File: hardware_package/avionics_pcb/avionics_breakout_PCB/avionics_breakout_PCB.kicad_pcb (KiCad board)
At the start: 2 copper layers, 5 parts, among them SW1 SW_Push

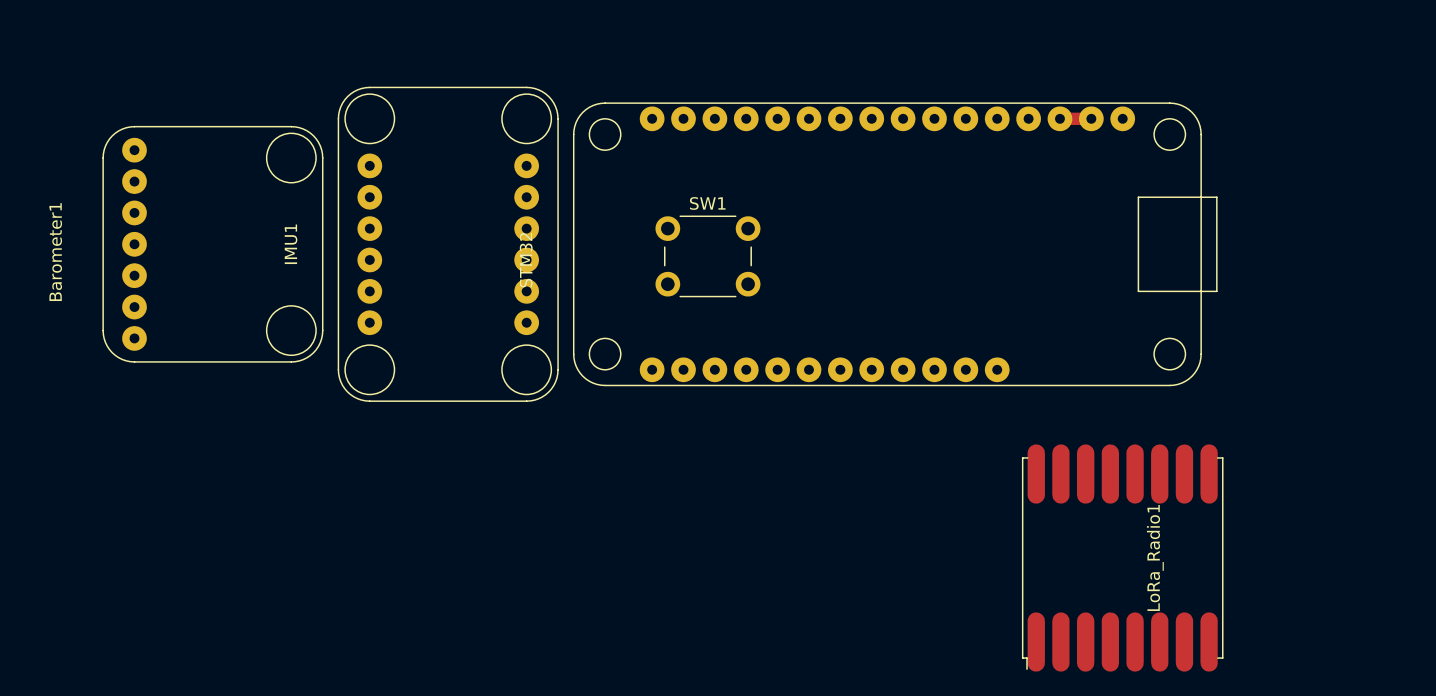
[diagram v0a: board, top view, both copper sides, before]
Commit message: Completed the PCB for the breakout board based avionics board. Also updated the CI/CD to include this new PCB
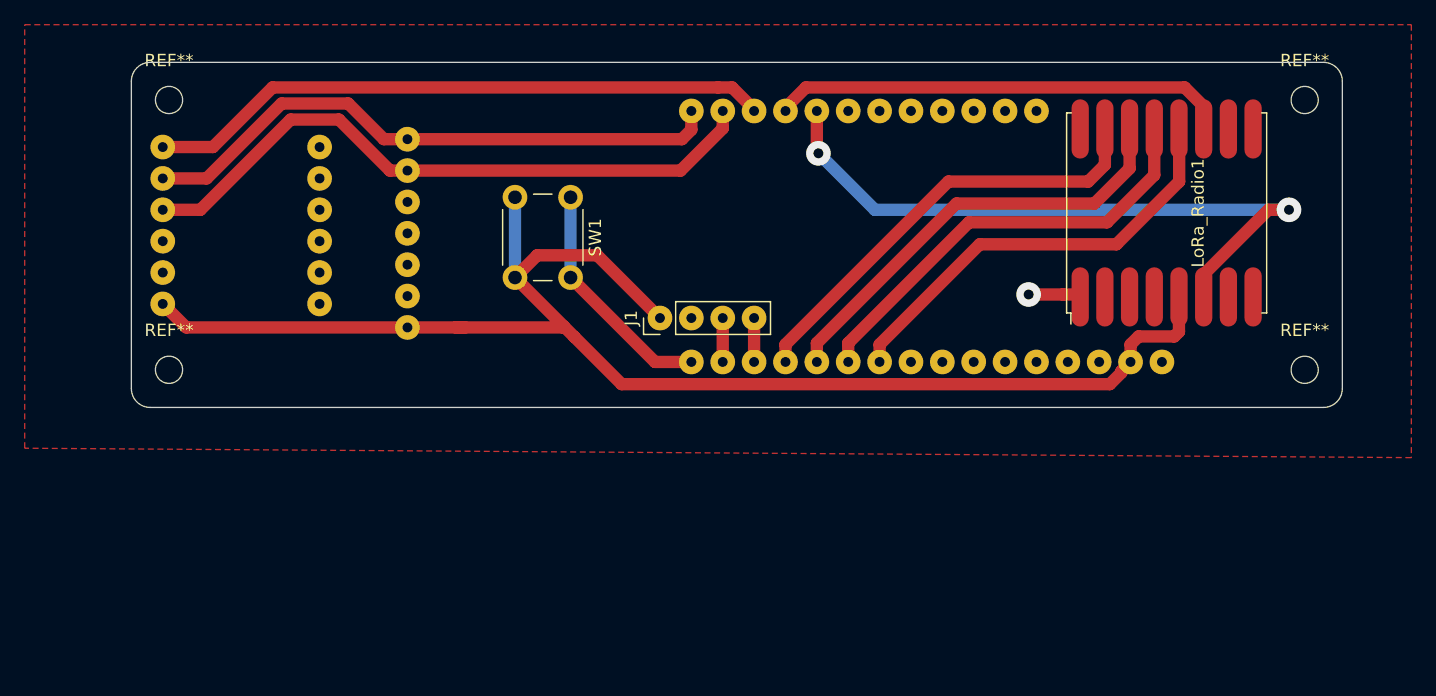
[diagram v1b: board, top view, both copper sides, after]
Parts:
- added J1: GPS, Connector_PinHeader_2.54mm:PinHeader_1x04_P2.54mm_Vertical, F.Cu at (76.8, 107.6)
- added REF**: MountingHole_2.2mm_M2, MountingHole:MountingHole_2.2mm_M2, F.Cu at (129.0, 111.8)
- added REF**: MountingHole_2.2mm_M2, MountingHole:MountingHole_2.2mm_M2, F.Cu at (129.0, 89.9)
- added REF**: MountingHole_2.2mm_M2, MountingHole:MountingHole_2.2mm_M2, F.Cu at (37.1, 89.9)
- added REF**: MountingHole_2.2mm_M2, MountingHole:MountingHole_2.2mm_M2, F.Cu at (37.1, 111.8)
- Barometer1, IMU1, STM32: moved to B.Cu
- moved LoRa_Radio1 28.2 mm to (117.9, 99.1)
- moved Barometer1 22.2 mm to (64.0, 100.1), turned to 90 degrees
- moved IMU1 16.8 mm to (41.7, 100.1), turned to 90 degrees
- moved SW1 8.27 mm to (69.6, 97.8), turned to 270 degrees
- moved STM32 3.24 mm to (69.2, 101.0), turned to 90 degrees
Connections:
- Barometer1 pad 1: 3V3 -> +3V3
- Barometer1 pad 3: Net-(Barometer1-Pad3) -> (no net)
- Barometer1 pad 4: Net-(Barometer1-Pad4) -> (no net)
- Barometer1 pad 5: Net-(Barometer1-Pad5) -> (no net)
- IMU1 pad 1: 3V3 -> +3V3
- IMU1 pad 10: Net-(IMU1-Pad10) -> (no net)
- IMU1 pad 11: Net-(IMU1-Pad11) -> (no net)
- IMU1 pad 12: Net-(IMU1-Pad12) -> (no net)
- IMU1 pad 2: Net-(IMU1-Pad2) -> (no net)
- IMU1 pad 6: Net-(IMU1-Pad6) -> INT_IMU
- IMU1 pad 7: Net-(IMU1-Pad7) -> GND
- IMU1 pad 8: Net-(IMU1-Pad8) -> (no net)
- IMU1 pad 9: Net-(IMU1-Pad9) -> (no net)
- LoRa_Radio1 pad 1: Net-(LoRa_Radio1-Pad1) -> (no net)
- LoRa_Radio1 pad 10: Net-(LoRa_Radio1-Pad10) -> (no net)
- LoRa_Radio1 pad 11: Net-(LoRa_Radio1-Pad11) -> RESET
- LoRa_Radio1 pad 12: Net-(LoRa_Radio1-Pad12) -> CS
- LoRa_Radio1 pad 13: Net-(LoRa_Radio1-Pad13) -> SCK
- LoRa_Radio1 pad 14: Net-(LoRa_Radio1-Pad14) -> MOSI
- LoRa_Radio1 pad 15: Net-(LoRa_Radio1-Pad15) -> MISO
- LoRa_Radio1 pad 16: Net-(LoRa_Radio1-Pad16) -> GND
- LoRa_Radio1 pad 3: Net-(LoRa_Radio1-Pad3) -> (no net)
- LoRa_Radio1 pad 4: Net-(LoRa_Radio1-Pad4) -> (no net)
- LoRa_Radio1 pad 5: 3V3 -> +3V3
- LoRa_Radio1 pad 6: Net-(LoRa_Radio1-Pad6) -> INT_LORA
- LoRa_Radio1 pad 7: Net-(LoRa_Radio1-Pad7) -> (no net)
- LoRa_Radio1 pad 8: Net-(LoRa_Radio1-Pad8) -> (no net)
- LoRa_Radio1 pad 9: Net-(LoRa_Radio1-Pad9) -> GND
- STM32 pad 1: Net-(STM32-Pad1) -> (no net)
- STM32 pad 10: Net-(STM32-Pad10) -> CS
- STM32 pad 11: Net-(STM32-Pad11) -> SCK
- STM32 pad 12: Net-(STM32-Pad12) -> MOSI
- STM32 pad 13: Net-(STM32-Pad13) -> MISO
- STM32 pad 14: Net-(STM32-Pad14) -> RX
- STM32 pad 15: Net-(STM32-Pad15) -> TX
- STM32 pad 19: Net-(STM32-Pad19) -> INT_IMU
- STM32 pad 2: 3V3 -> +3V3
- STM32 pad 20: Net-(STM32-Pad20) -> RESET
- STM32 pad 21: Net-(STM32-Pad21) -> INT_LORA
- STM32 pad 22: Net-(STM32-Pad22) -> (no net)
- STM32 pad 23: Net-(STM32-Pad23) -> (no net)
- STM32 pad 24: Net-(STM32-Pad24) -> (no net)
- STM32 pad 25: Net-(STM32-Pad25) -> (no net)
- STM32 pad 26: Net-(STM32-Pad26) -> (no net)
- STM32 pad 27: Net-(STM32-Pad27) -> (no net)
- STM32 pad 28: Net-(STM32-Pad28) -> (no net)
- STM32 pad 3: 3V3 -> (no net)
- STM32 pad 5: Net-(STM32-Pad5) -> (no net)
- STM32 pad 6: Net-(STM32-Pad6) -> (no net)
- STM32 pad 7: Net-(STM32-Pad7) -> (no net)
- STM32 pad 8: Net-(STM32-Pad8) -> (no net)
- STM32 pad 9: Net-(STM32-Pad9) -> (no net)
- SW1 pad 2: 3V3 -> +3V3
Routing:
- net +3V3: track 0.00 -> 116.7 mm
- net INT_LORA: track 0.00 -> 55.6 mm, vias 0 -> 2
- net SCL: track 0.00 -> 52.9 mm
- net INT_IMU: track 0.00 -> 50.7 mm
- net SDA: track 0.00 -> 48.3 mm
- net SCK: track 0.00 -> 37.6 mm
- net MISO: track 0.00 -> 37.4 mm
- net MOSI: track 0.00 -> 37.2 mm
- net CS: track 0.00 -> 36.6 mm
- net RESET: track 0.00 -> 36.2 mm
- net Boot: track 0.00 -> 19.1 mm
- net (no net): track 0.00 -> 5.51 mm, vias 0 -> 1
- net GND: track 0.00 -> 5.41 mm
- net TX: track 0.00 -> 3.56 mm
- net RX: track 0.00 -> 3.56 mm
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- added copper zone on F.Cu, net GND
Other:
- board outline added: 98 x 27.9 mm

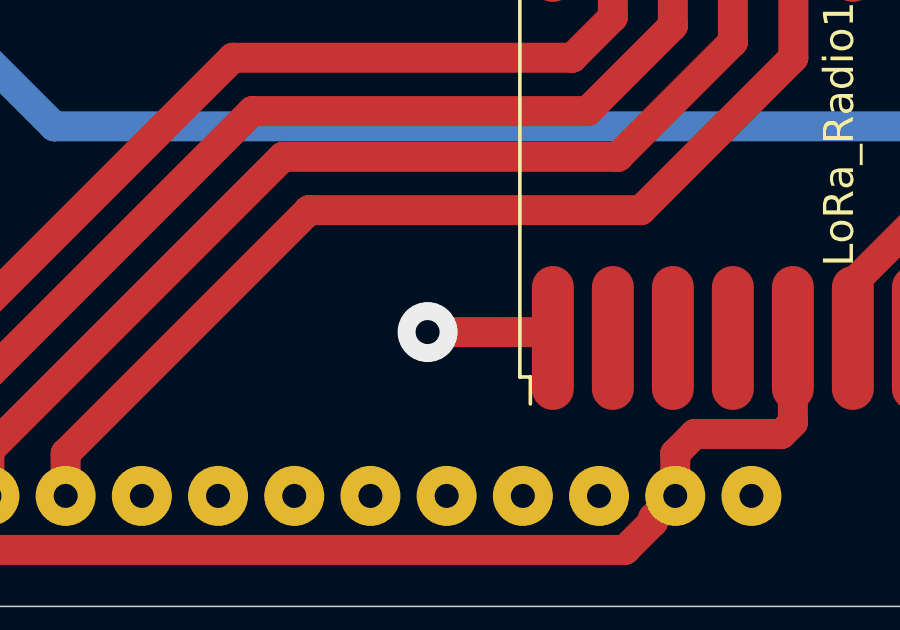
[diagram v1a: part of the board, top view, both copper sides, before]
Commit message: Fixed DRC check errors
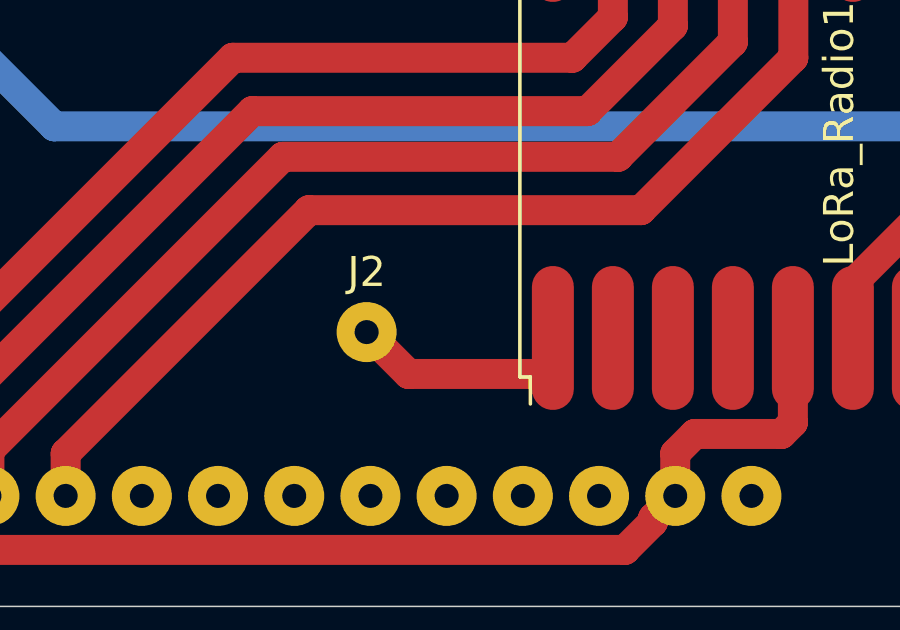
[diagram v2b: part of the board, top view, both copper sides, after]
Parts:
- added J2: ANT, Connector_Wire:SolderWire-0.1sqmm_1x01_D0.4mm_OD1mm, F.Cu at (104.6, 105.7)
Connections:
- LoRa_Radio1 pad 1: (no net) -> Net-(J2-Pad1)
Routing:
- net Net-(J2-Pad1): track 0.00 -> 6.79 mm
- net (no net): track 5.51 -> 0.00 mm, vias 1 -> 0

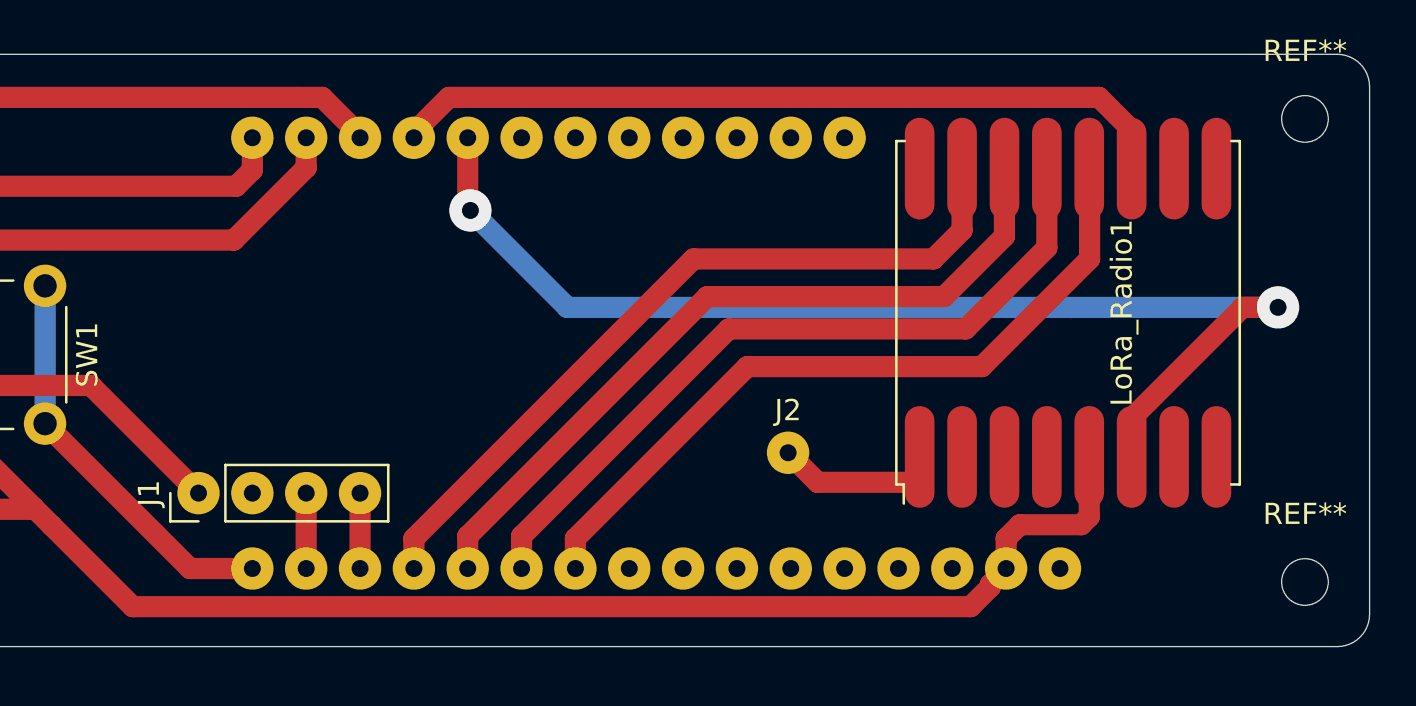
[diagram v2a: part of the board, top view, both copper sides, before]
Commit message: Added servo data connections, as well as ingnition charge data lines
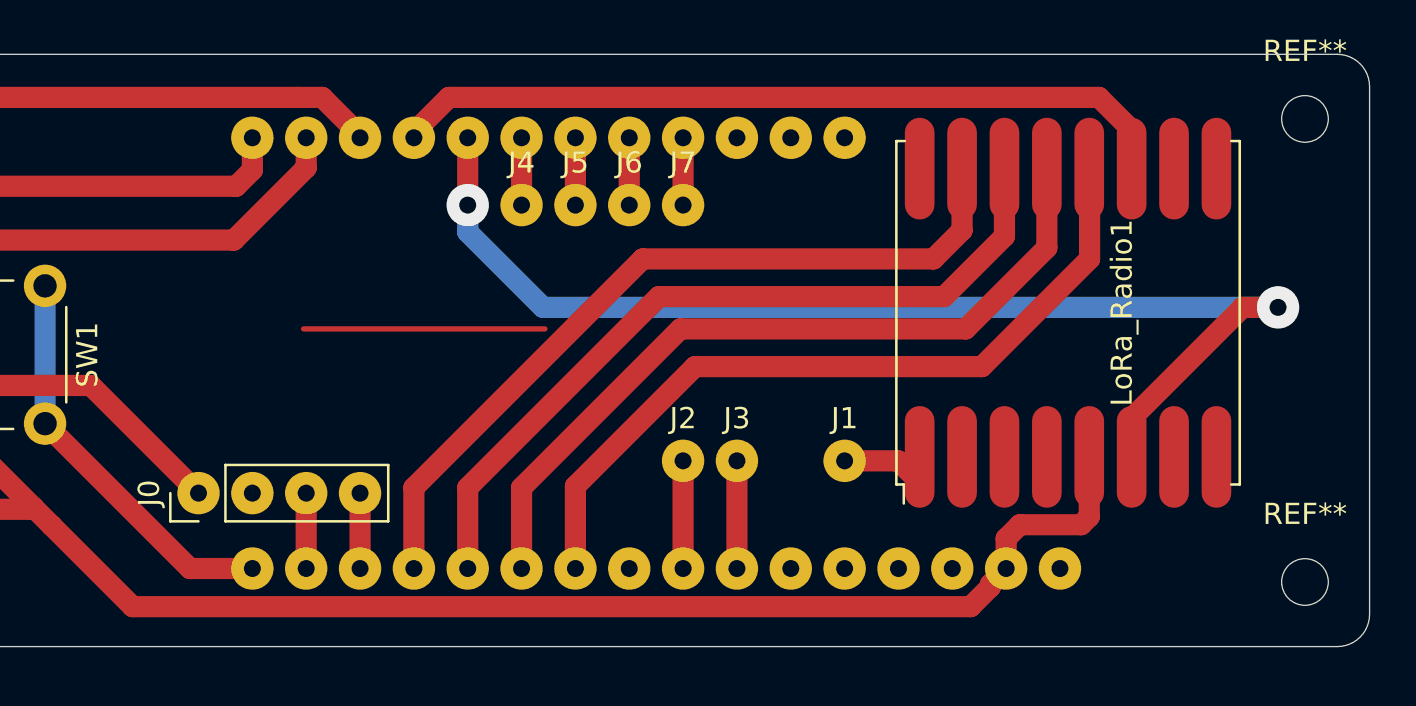
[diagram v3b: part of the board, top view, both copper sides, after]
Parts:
- added J1: ANT, Connector_Wire:SolderWire-0.1sqmm_1x01_D0.4mm_OD1mm, F.Cu at (107.3, 106.0)
- added J3: SER_2, Connector_Wire:SolderWire-0.1sqmm_1x01_D0.4mm_OD1mm, F.Cu at (102.2, 106.0)
- added J4: IGN_1, Connector_Wire:SolderWire-0.1sqmm_1x01_D0.4mm_OD1mm, F.Cu at (92.1, 94.0)
- added J5: IGN_2, Connector_Wire:SolderWire-0.1sqmm_1x01_D0.4mm_OD1mm, F.Cu at (94.6, 94.0)
- added J6: IGN_3, Connector_Wire:SolderWire-0.1sqmm_1x01_D0.4mm_OD1mm, F.Cu at (97.2, 94.0)
- added J7: IGN_4, Connector_Wire:SolderWire-0.1sqmm_1x01_D0.4mm_OD1mm, F.Cu at (99.7, 94.0)
- J2: value ANT -> SER_1
- moved J2 4.97 mm to (99.7, 106.0)
- renumbered J1 to J0
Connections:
- Barometer1 pad 3: (no net) -> Net-(Barometer1-Pad3)
- Barometer1 pad 4: (no net) -> Net-(Barometer1-Pad4)
- Barometer1 pad 5: (no net) -> Net-(Barometer1-Pad5)
- IMU1 pad 10: (no net) -> Net-(IMU1-Pad10)
- IMU1 pad 11: (no net) -> Net-(IMU1-Pad11)
- IMU1 pad 12: (no net) -> Net-(IMU1-Pad12)
- IMU1 pad 2: (no net) -> Net-(IMU1-Pad2)
- IMU1 pad 8: (no net) -> Net-(IMU1-Pad8)
- IMU1 pad 9: (no net) -> Net-(IMU1-Pad9)
- LoRa_Radio1 pad 1: Net-(J2-Pad1) -> Net-(J1-Pad1)
- LoRa_Radio1 pad 10: (no net) -> Net-(LoRa_Radio1-Pad10)
- LoRa_Radio1 pad 3: (no net) -> Net-(LoRa_Radio1-Pad3)
- LoRa_Radio1 pad 4: (no net) -> Net-(LoRa_Radio1-Pad4)
- LoRa_Radio1 pad 7: (no net) -> Net-(LoRa_Radio1-Pad7)
- LoRa_Radio1 pad 8: (no net) -> Net-(LoRa_Radio1-Pad8)
- STM32 pad 1: (no net) -> Net-(STM32-Pad1)
- STM32 pad 22: (no net) -> Net-(J4-Pad1)
- STM32 pad 23: (no net) -> Net-(J5-Pad1)
- STM32 pad 24: (no net) -> Net-(J6-Pad1)
- STM32 pad 25: (no net) -> Net-(J7-Pad1)
- STM32 pad 26: (no net) -> Net-(STM32-Pad26)
- STM32 pad 27: (no net) -> Net-(STM32-Pad27)
- STM32 pad 28: (no net) -> Net-(STM32-Pad28)
- STM32 pad 3: (no net) -> Net-(STM32-Pad3)
- STM32 pad 5: (no net) -> Net-(STM32-Pad5)
- STM32 pad 6: (no net) -> Net-(STM32-Pad6)
- STM32 pad 7: (no net) -> Net-(J3-Pad1)
- STM32 pad 8: (no net) -> Net-(J2-Pad1)
- STM32 pad 9: (no net) -> Net-(STM32-Pad9)
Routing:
- net (no net): track 0.00 -> 11.4 mm
- net Net-(J3-Pad1): track 0.00 -> 5.08 mm
- net Net-(J1-Pad1): track 0.00 -> 3.96 mm
- net Net-(J7-Pad1): track 0.00 -> 3.17 mm
- net Net-(J6-Pad1): track 0.00 -> 3.17 mm
- net Net-(J5-Pad1): track 0.00 -> 3.17 mm
- net Net-(J4-Pad1): track 0.00 -> 3.17 mm
- net Net-(J2-Pad1): track 6.79 -> 5.08 mm
- net CS: track 36.6 -> 38.0 mm
- net MISO: track 37.4 -> 38.8 mm
- net SCK: track 37.6 -> 38.9 mm
- net MOSI: track 37.2 -> 38.6 mm
- net INT_LORA: track 55.6 -> 56.4 mm

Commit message: Updated ground plane
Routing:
- net (no net): track 11.4 -> 0.00 mm

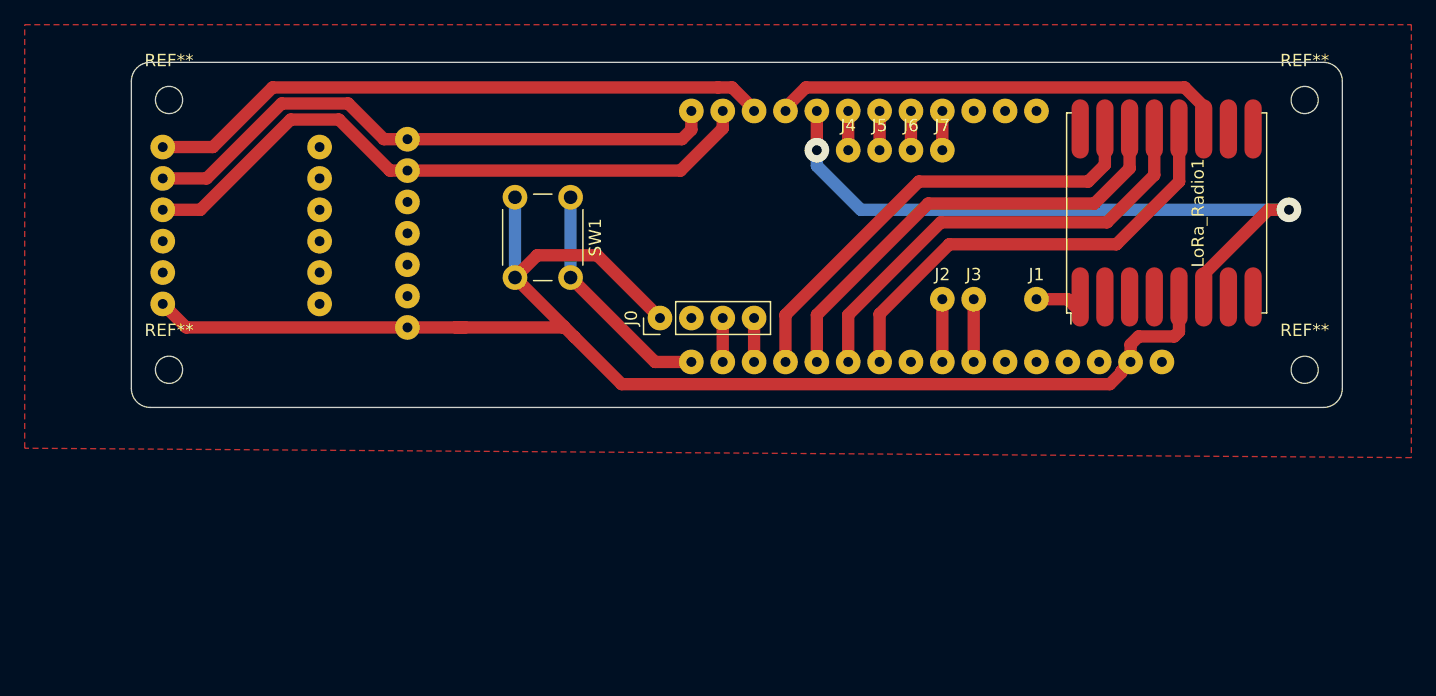
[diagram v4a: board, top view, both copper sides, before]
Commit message: Finalised the breakout board PCB
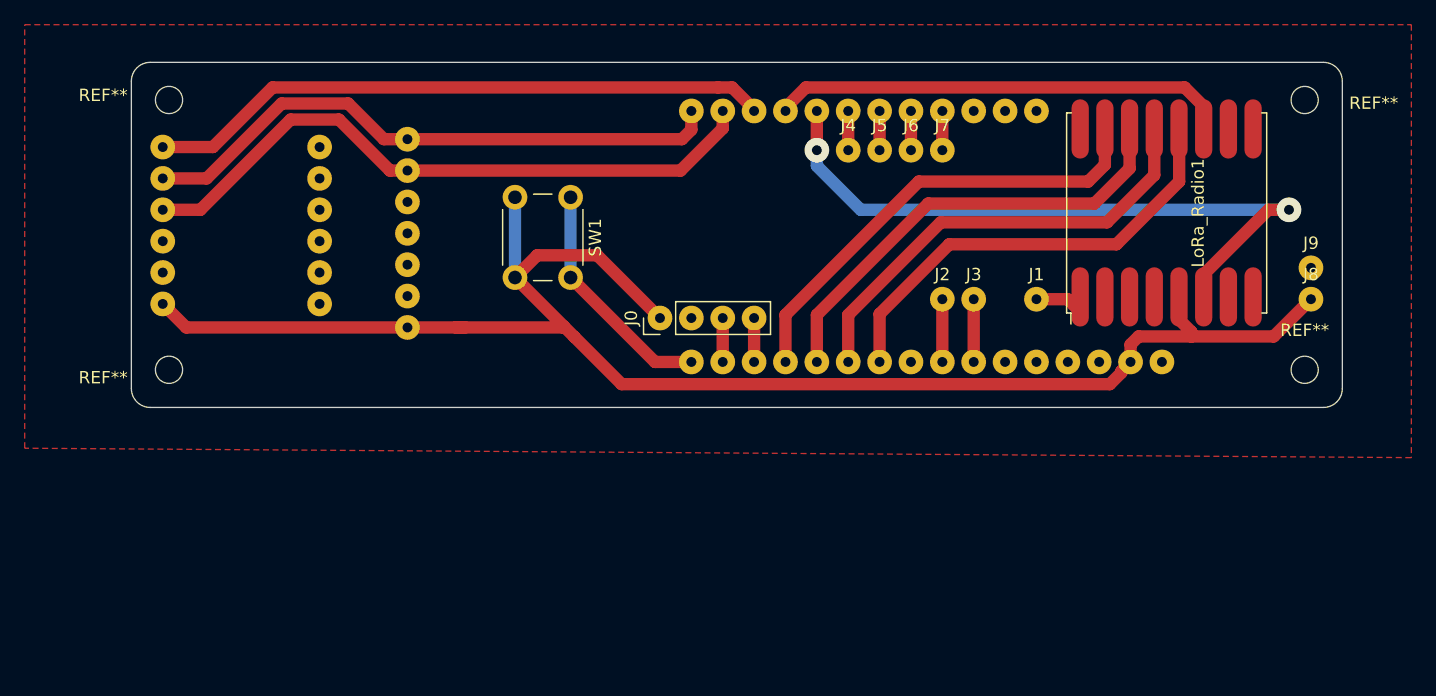
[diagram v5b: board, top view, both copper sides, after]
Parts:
- added J8: 3V3_IN, Connector_Wire:SolderWire-0.1sqmm_1x01_D0.4mm_OD1mm, F.Cu at (129.5, 106.0)
- added J9: GND_IN, Connector_Wire:SolderWire-0.1sqmm_1x01_D0.4mm_OD1mm, F.Cu at (129.5, 103.5)
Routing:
- net +3V3: track 116.7 -> 129.3 mm
